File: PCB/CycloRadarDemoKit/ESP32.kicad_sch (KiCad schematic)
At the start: 19 parts, among them SW101 RESET, SW102 BOOT MODE, U101 ESP32-WROVER-E-N16R8

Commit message: JLCPCB mistakes repaired, cosmetics on PCB
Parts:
- R106: LCSC C25804 -> (none); now left out of the parts list
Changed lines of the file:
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@@
   )
   (symbol (lib_id "Device:R") (at 219.71 105.41 0) (mirror y) (unit 1)
-    (in_bom yes) (on_board yes) (dnp yes)
+    (in_bom no) (on_board yes) (dnp yes)
     (property "Reference" "R106" (at 217.17 104.14 0)
       (effects (font (size 1.27 1.27)) (justify left))
@@
       (effects (font (size 1.27 1.27)) hide)
     )
-    (property "LCSC" "C25804" (at 219.71 105.41 0)
-      (effects (font (size 1.27 1.27)) hide)
-    )

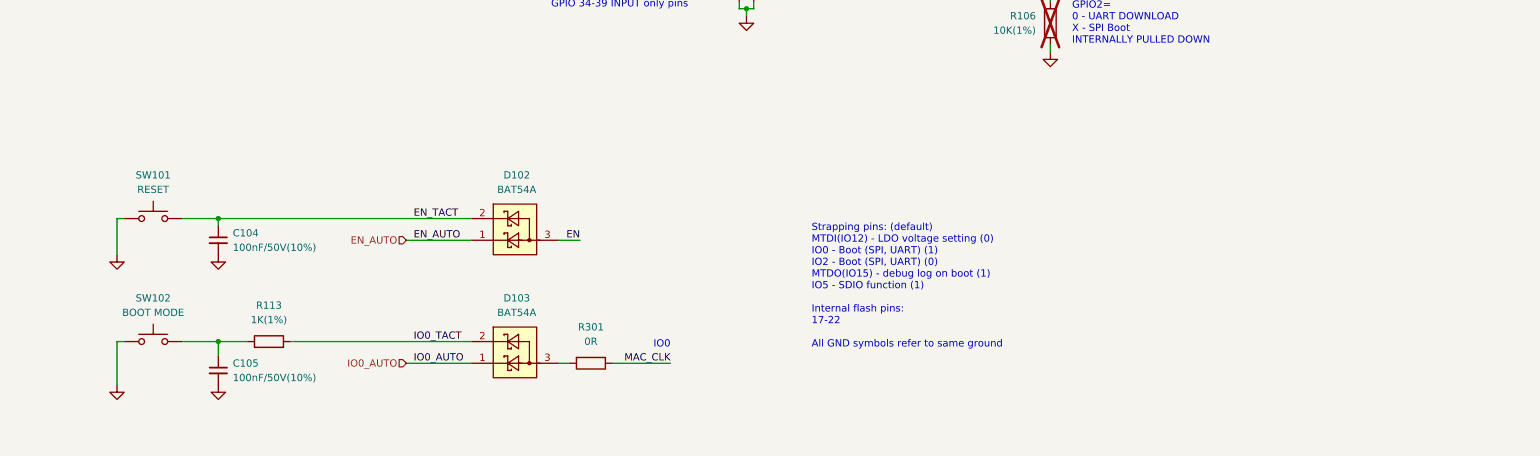
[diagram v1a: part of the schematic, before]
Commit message: Sematic Versioning implemented, whish list added
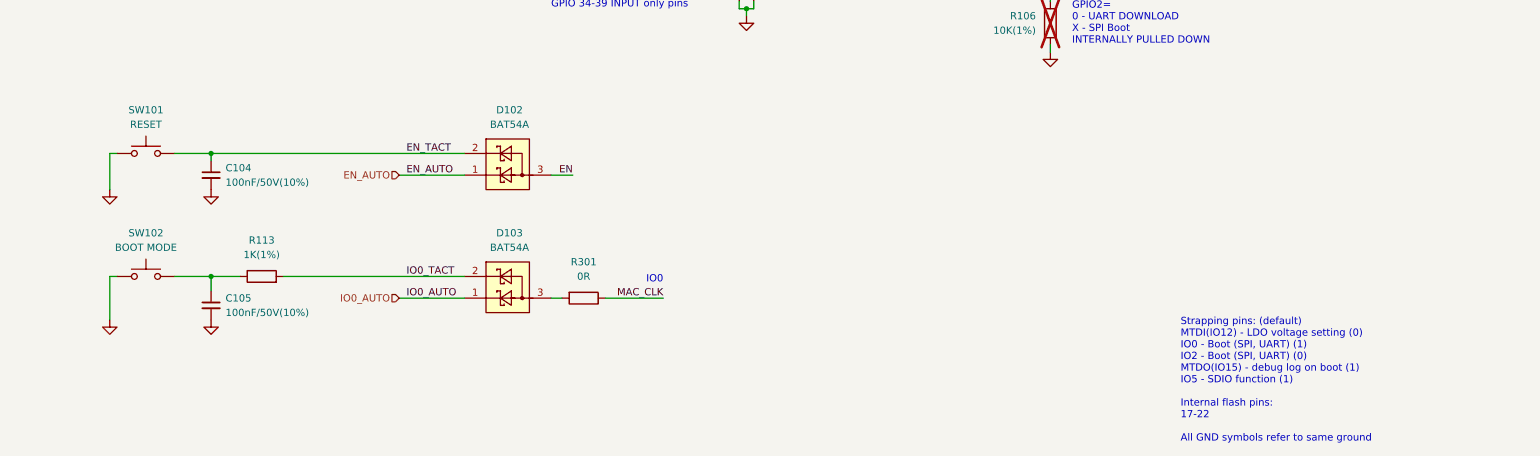
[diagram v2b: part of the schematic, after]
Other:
- company: ALPS Electric Czech, s.r.o. -> ${COMPANY}
- title: Radar Safety Sensor -> ${TITLE}
- moved on the sheet: C104, C105, D102, D103, R113, R301, SW101, SW102

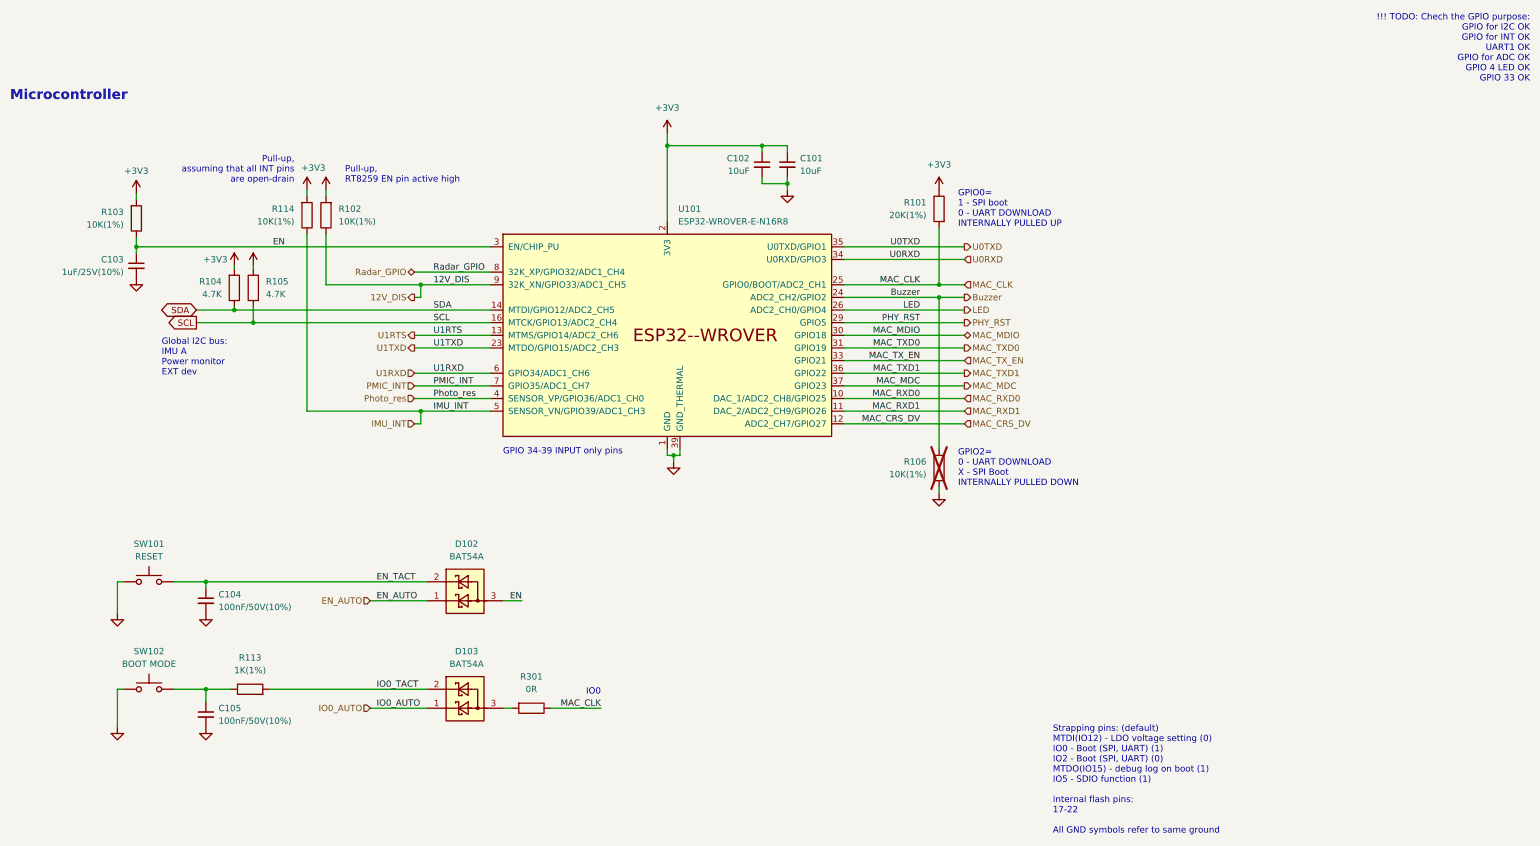
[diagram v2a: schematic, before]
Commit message: photos added, readme rewrited
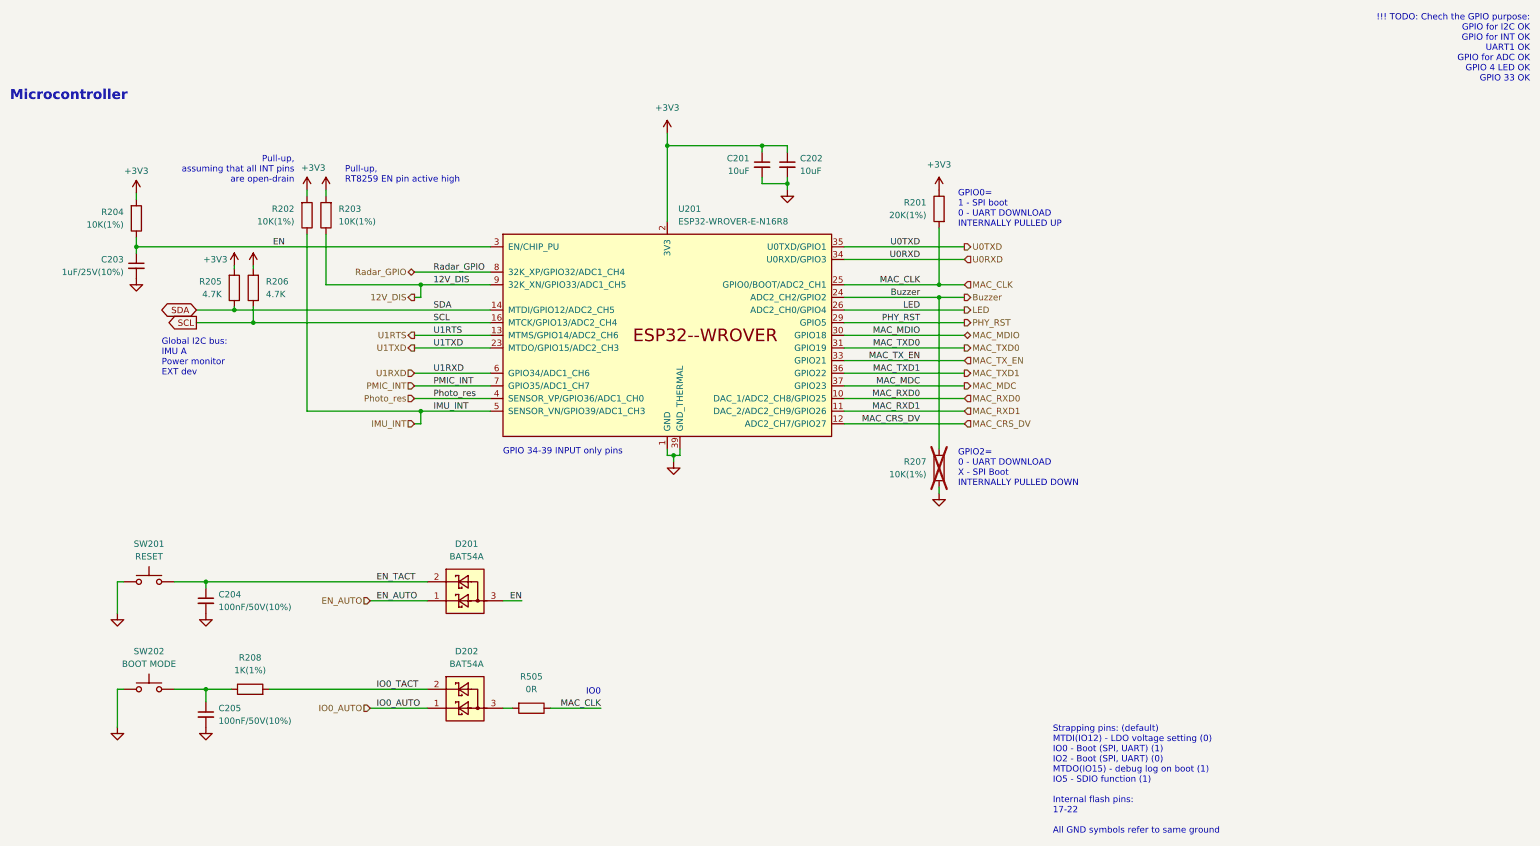
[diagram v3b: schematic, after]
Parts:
- renumbered C102 to C201, C101 to C202, C103 to C203, C104 to C204, C105 to C205, D102 to D201, D103 to D202, R101 to R201, R114 to R202, R102 to R203, R103 to R204, R104 to R205, R105 to R206, R106 to R207, R113 to R208, R301 to R505, SW101 to SW201, SW102 to SW202, U101 to U201
